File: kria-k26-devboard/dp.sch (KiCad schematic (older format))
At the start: 26 parts

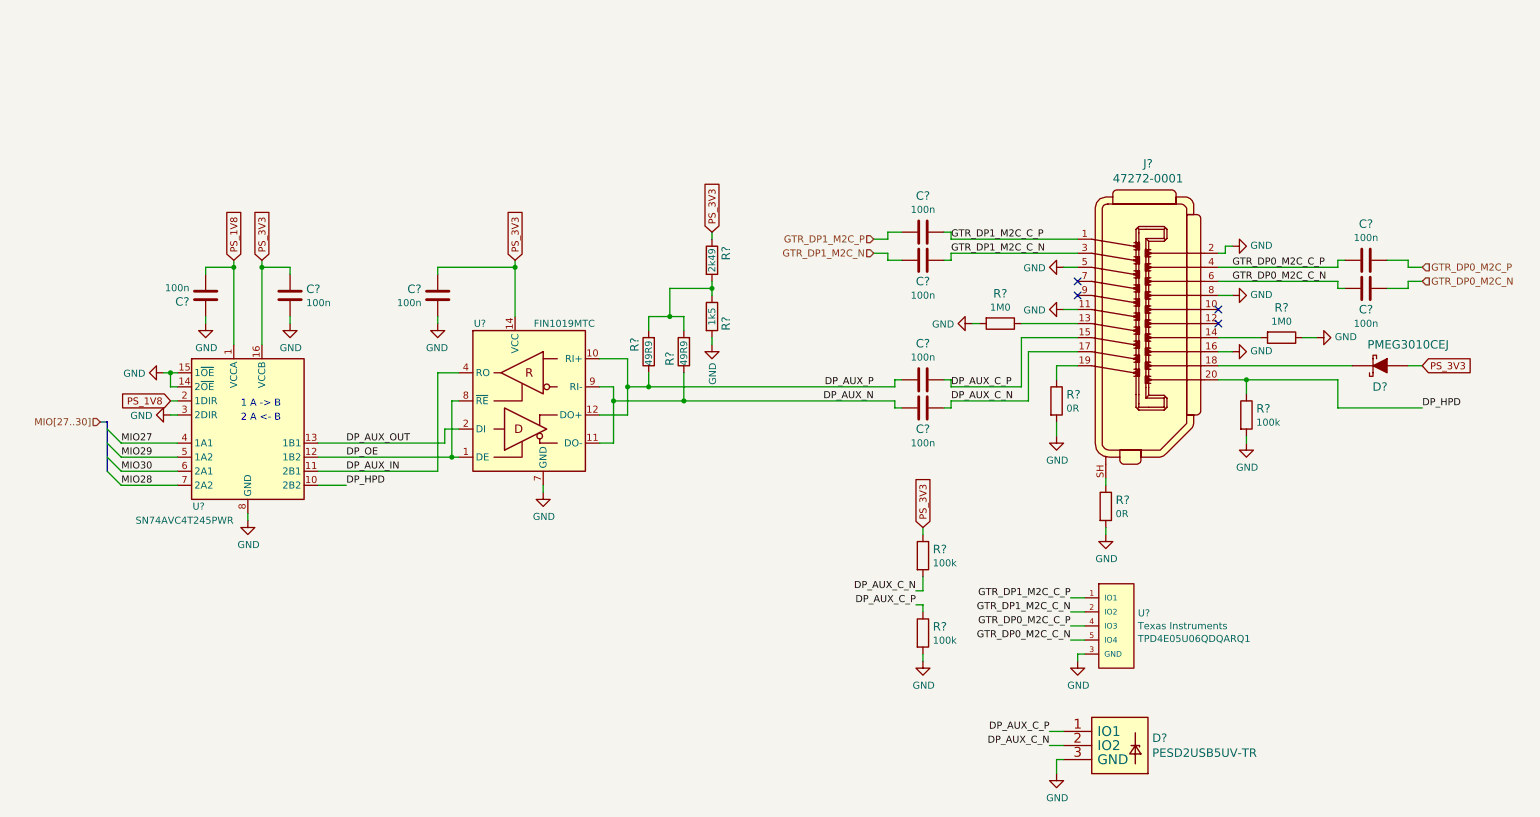
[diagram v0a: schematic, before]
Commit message: Finished reset logic, added crystal gen. to USB PHY, create power toggle for SD 3.0
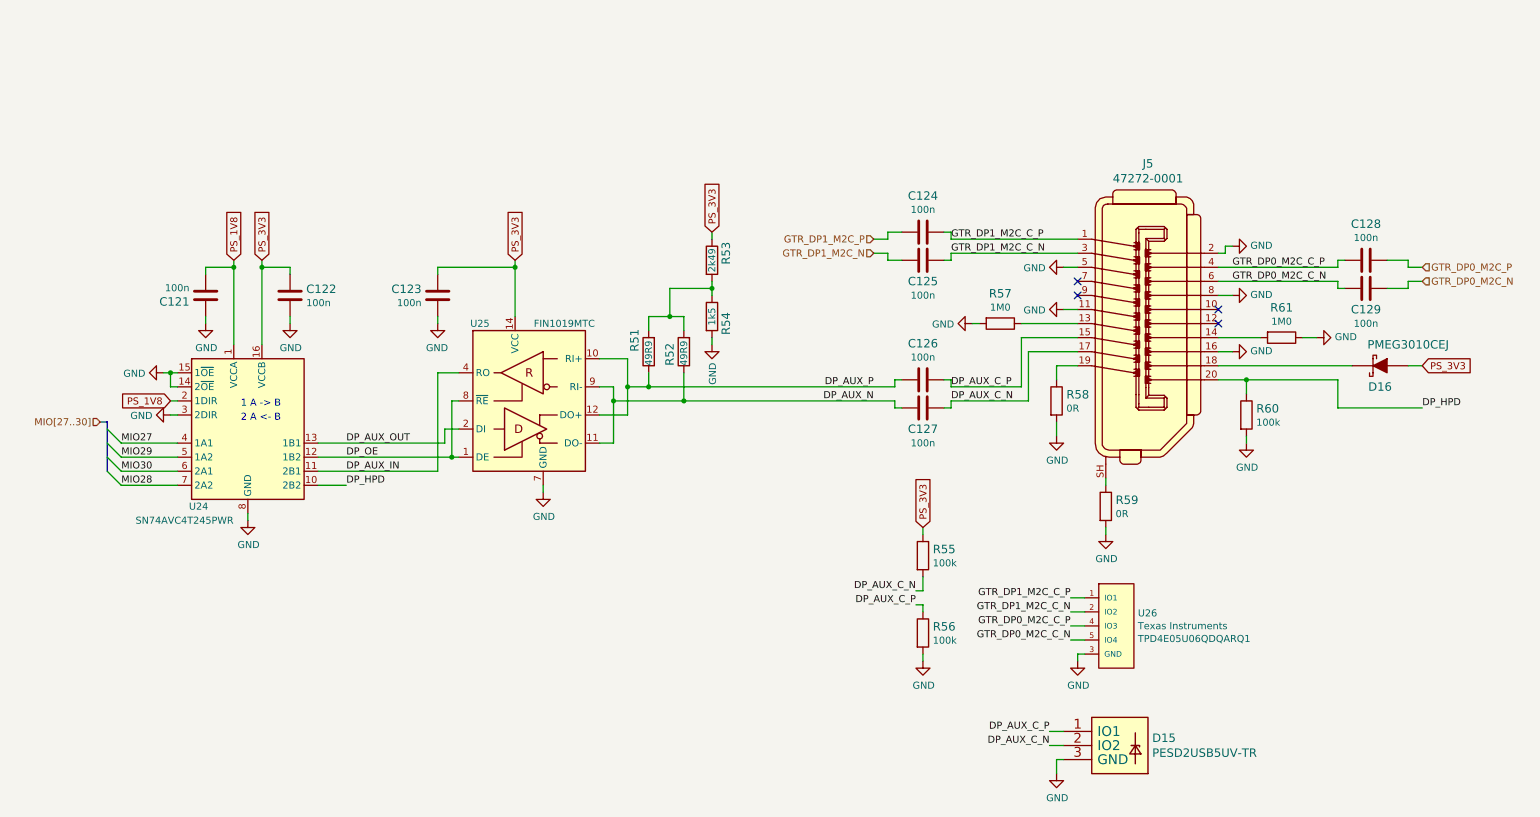
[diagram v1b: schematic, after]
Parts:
- gave numbers to parts that had none: 26

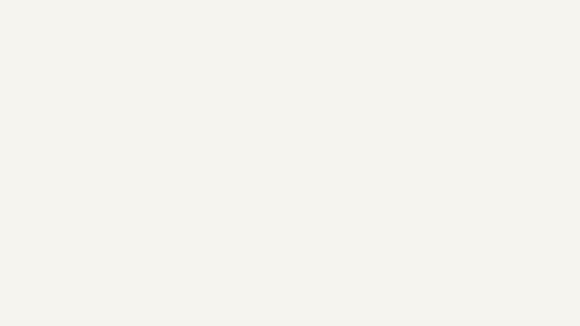
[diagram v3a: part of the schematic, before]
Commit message: Finished tidying up the schematic
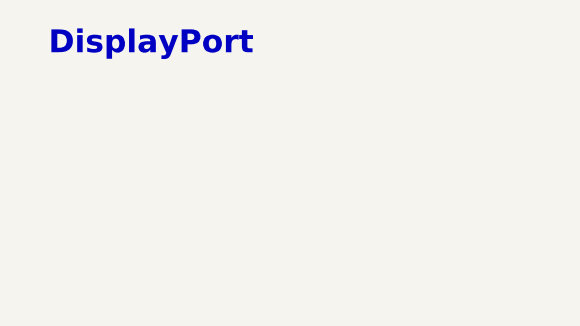
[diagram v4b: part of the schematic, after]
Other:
- note added: "DisplayPort"
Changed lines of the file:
@@
 $Descr A4 11693 8268
 encoding utf-8
-Sheet 10 19
+Sheet 3 19
 Title ""
 Date "2022-03-10"
@@
 Wire Bus Line
 	1100 3500 1100 3850
+Text Notes 550  750  0    100  ~ 20
+DisplayPort
 $EndSCHEMATC

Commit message: Progress in PCB placement
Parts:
- U1: renamed from U24; footprint Package_SO:TSSOP-16_4.4x5mm_P0.65mm -> antmicro-footprints:TSSOP-16_4.4x5mm_P0.65mm
- renumbered C124 to C10, C125 to C11, C126 to C12, C127 to C13, C128 to C14, C129 to C15, C121 to C7, C122 to C8, C123 to C9, D15 to D1, D16 to D2, J5 to J1, R57 to R10, R58 to R11, R59 to R12, R60 to R13, R61 to R14, R51 to R4, R52 to R5, R53 to R6, R54 to R7, R55 to R8, R56 to R9, U25 to U2, U26 to U3

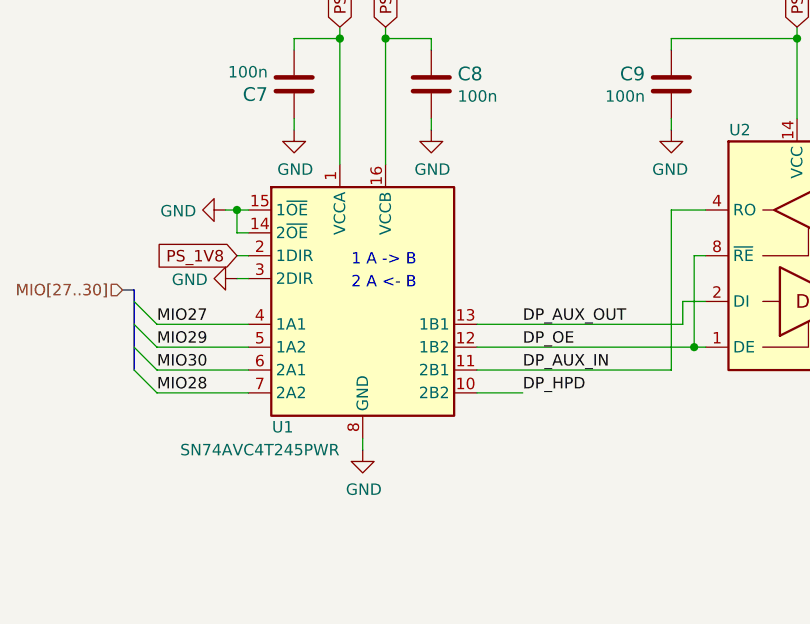
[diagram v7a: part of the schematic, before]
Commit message: Component size optimization, SOM connector fanout, routing of camera interface
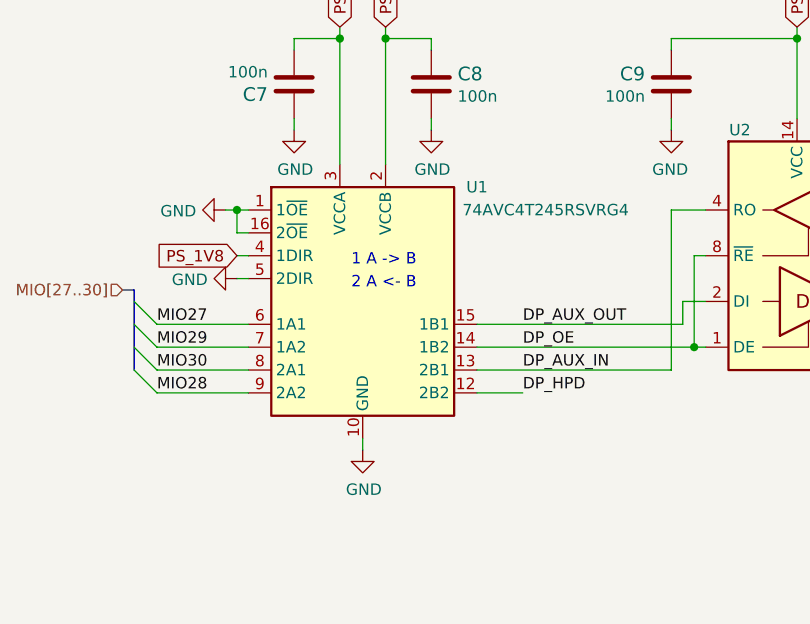
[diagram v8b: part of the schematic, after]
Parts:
- removed U1: SN74AVC4T245PWR, antmicro-footprints:TSSOP-16_4.4x5mm_P0.65mm, symbol antmicroLogicTranslatorsLevelShifters:SN74AVC4T245PWR
- added U1: 74AVC4T245RSVRG4, antmicro-footprints:Texas_16-UFQFN, symbol antmicroLogicTranslatorsLevelShifters:74AVC4T245RSVRG4
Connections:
- net DP_AUX_IN: now also U1.13 (2B1)
- net DP_AUX_OUT: now also U1.15 (1B1)
- net DP_HPD: now also U1.12 (2B2)
- net DP_OE: now also U1.14 (1B2)
- net GND: now also U1.1 (1~OE), U1.10 (GND), U1.11 (GND), U1.16 (2~OE), U1.5 (2DIR)
- net MIO27: now also U1.6 (1A1)
- net MIO28: now also U1.9 (2A2)
- net MIO29: now also U1.7 (1A2)
- net MIO30: now also U1.8 (2A1)
- net PS_1V8: now also U1.3 (VCCA), U1.4 (1DIR)
- net PS_3V3: now also U1.2 (VCCB)
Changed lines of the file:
@@
-	1    0    0    -1
-$EndComp
-$Comp
-L antmicroLogicTranslatorsLevelShifters:SN74AVC4T245PWR U1
-U 1 1 63C4DF6B
-P 2100 3550
-F 0 "U1" H 1750 3000 50  0000 C CNN
-F 1 "SN74AVC4T245PWR" H 1650 2900 50  0000 C CNN
-F 2 "antmicro-footprints:TSSOP-16_4.4x5mm_P0.65mm" H 2100 3450 50  0001 C CNN
-F 3 "https://www.ti.com/lit/ds/symlink/sn74avc4t245.pdf" H 2050 3300 50  0001 C CNN
-	1    2100 3550
 	1    0    0    -1
 $EndComp
@@
 Wire Bus Line
 	1100 3500 1100 3850
+$Comp
+L antmicroLogicTranslatorsLevelShifters:74AVC4T245RSVRG4 U1
+U 1 1 635038ED
+P 2100 3550
+F 0 "U1" H 2600 4050 50  0000 C CNN
+F 1 "74AVC4T245RSVRG4" H 2900 3950 50  0000 C CNN
+F 2 "antmicro-footprints:Texas_16-UFQFN" H 2900 2800 50  0001 C CNN
+F 3 "https://www.ti.com/lit/ds/symlink/sn74avc4t245.pdf" H 2050 3300 50  0001 C CNN
+F 4 "74AVC4T245RSVRG4" H 2550 2900 50  0001 C CNN "MPN"
+F 5 "Texas Instruments" H 2500 3000 50  0001 C CNN "Manufacturer"
+	1    2100 3550
+	1    0    0    -1
+$EndComp
 $EndSCHEMATC
